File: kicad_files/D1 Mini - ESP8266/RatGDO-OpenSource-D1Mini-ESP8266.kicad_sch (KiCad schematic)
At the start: 7 parts, among them J1 Screw_Terminal_01x03, Q1 2N7002, Q2 AO3400A, U1 WeMos_D1_mini

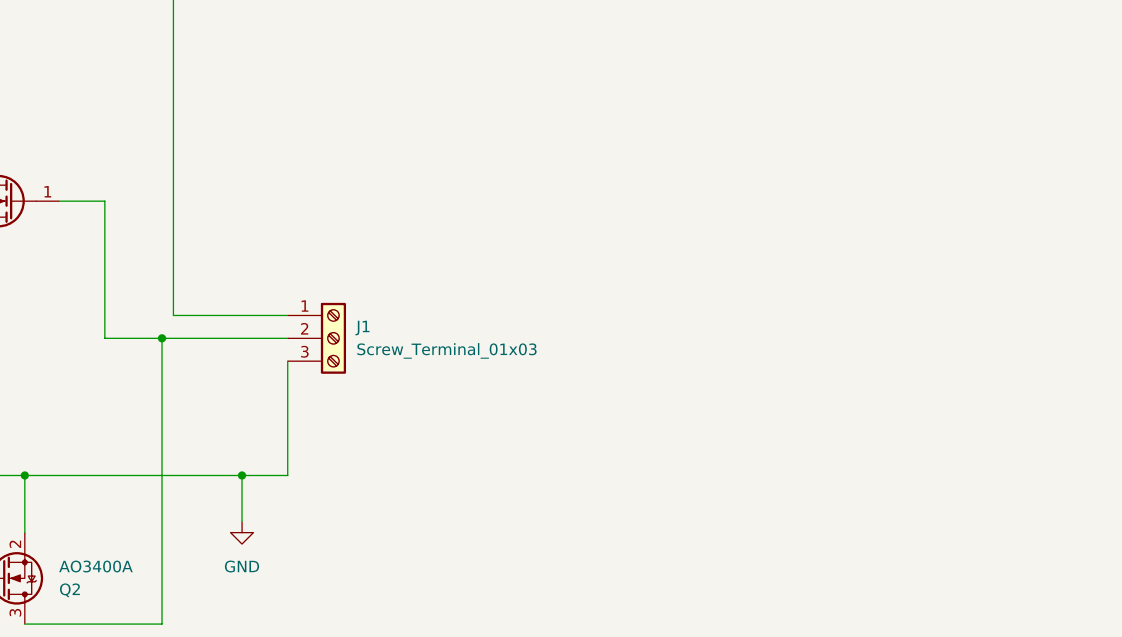
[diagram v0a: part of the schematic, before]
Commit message: Fixed Bad PCB Labeling
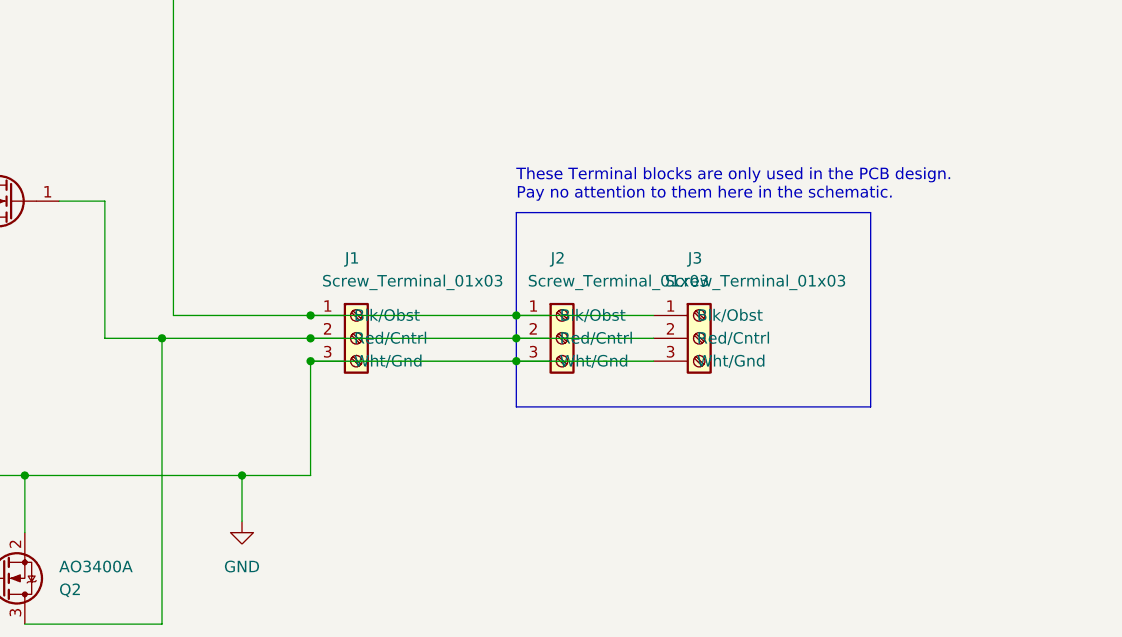
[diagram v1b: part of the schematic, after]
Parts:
- added J2: Screw_Terminal_01x03, Connector_Phoenix_MC:PhoenixContact_MCV_1,5_3-G-3.5_1x03_P3.50mm_Vertical, symbol Connector:Screw_Terminal_01x03
- added J3: Screw_Terminal_01x03, Connector_PinHeader_2.54mm:PinHeader_1x03_P2.54mm_Vertical, symbol Connector:Screw_Terminal_01x03
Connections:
- net GND: now also J2.3 (Wht/Gnd), J3.3 (Wht/Gnd)
- net at J1.1 (Blk/Obst), R1.1: now also J2.1 (Blk/Obst), J3.1 (Blk/Obst)
- net at J1.2 (Red/Cntrl), Q1.1 (G), Q2.3 (D): now also J2.2 (Red/Cntrl), J3.2 (Red/Cntrl)
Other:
- note added: "These Terminal blocks are only used in the PCB design. Pay no attention to them here in the schematic."
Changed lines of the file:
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@@
 (kicad_sch (version 20230121) (generator eeschema)
   (paper "A4")
+  (junction (at 160.02 87.63) (diameter 0) (color 0 0 0 0)
+  )
+  (junction (at 182.88 87.63) (diameter 0) (color 0 0 0 0)
+  )
   (junction (at 152.4 105.41) (diameter 0) (color 0 0 0 0)
   )
+  (junction (at 160.02 92.71) (diameter 0) (color 0 0 0 0)
+  )
   (junction (at 105.41 105.41) (diameter 0) (color 0 0 0 0)
   )
+  (junction (at 160.02 90.17) (diameter 0) (color 0 0 0 0)
+  )
   (junction (at 128.27 105.41) (diameter 0) (color 0 0 0 0)
   )
+  (junction (at 182.88 92.71) (diameter 0) (color 0 0 0 0)
+  )
+  (junction (at 182.88 90.17) (diameter 0) (color 0 0 0 0)
+  )
   (junction (at 105.41 69.85) (diameter 0) (color 0 0 0 0)
   )
@@
   (junction (at 105.41 116.84) (diameter 0) (color 0 0 0 0)
   )
+  (wire (pts (xy 182.88 87.63) (xy 198.12 87.63))
+    (stroke (width 0) (type default))
+  )
   (wire (pts (xy 128.27 121.92) (xy 143.51 121.92))
     (stroke (width 0) (type default))
@@
     (stroke (width 0) (type default))
   )
+  (polyline (pts (xy 182.88 76.2) (xy 222.25 76.2))
+    (stroke (width 0) (type default))
+  )
   (wire (pts (xy 143.51 90.17) (xy 137.16 90.17))
     (stroke (width 0) (type default))
@@
     (stroke (width 0) (type default))
   )
+  (wire (pts (xy 160.02 90.17) (xy 182.88 90.17))
+    (stroke (width 0) (type default))
+  )
   (wire (pts (xy 113.03 52.07) (xy 144.78 52.07))
     (stroke (width 0) (type default))
   )
+  (polyline (pts (xy 182.88 97.79) (xy 222.25 97.79))
+    (stroke (width 0) (type default))
+  )
   (wire (pts (xy 90.17 80.01) (xy 124.46 80.01))
     (stroke (width 0) (type default))
@@
     (stroke (width 0) (type default))
   )
+  (wire (pts (xy 160.02 87.63) (xy 182.88 87.63))
+    (stroke (width 0) (type default))
+  )
   (wire (pts (xy 105.41 52.07) (xy 95.25 52.07))
     (stroke (width 0) (type default))
@@
     (stroke (width 0) (type default))
   )
-  (wire (pts (xy 157.48 92.71) (xy 157.48 105.41))
+  (wire (pts (xy 160.02 92.71) (xy 160.02 105.41))
     (stroke (width 0) (type default))
   )
@@
     (stroke (width 0) (type default))
   )
+  (polyline (pts (xy 222.25 97.79) (xy 222.25 76.2))
+    (stroke (width 0) (type default))
+  )
   (wire (pts (xy 92.71 77.47) (xy 92.71 116.84))
     (stroke (width 0) (type default))
   )
+  (wire (pts (xy 160.02 92.71) (xy 182.88 92.71))
+    (stroke (width 0) (type default))
+  )
   (wire (pts (xy 152.4 105.41) (xy 152.4 110.49))
     (stroke (width 0) (type default))
@@
     (stroke (width 0) (type default))
   )
+  (wire (pts (xy 182.88 92.71) (xy 198.12 92.71))
+    (stroke (width 0) (type default))
+  )
   (wire (pts (xy 105.41 69.85) (xy 124.46 69.85))
     (stroke (width 0) (type default))
   )
+  (wire (pts (xy 182.88 90.17) (xy 198.12 90.17))
+    (stroke (width 0) (type default))
+  )
+  (polyline (pts (xy 182.88 76.2) (xy 182.88 97.79))
+    (stroke (width 0) (type default))
+  )
   (wire (pts (xy 82.55 57.15) (xy 82.55 64.77))
     (stroke (width 0) (type default))
@@
     (stroke (width 0) (type default))
   )
+  (wire (pts (xy 143.51 90.17) (xy 160.02 90.17))
+    (stroke (width 0) (type default))
+  )
   (wire (pts (xy 105.41 69.85) (xy 105.41 105.41))
     (stroke (width 0) (type default))
@@
     (stroke (width 0) (type default))
   )
-  (wire (pts (xy 144.78 87.63) (xy 157.48 87.63))
-    (stroke (width 0) (type default))
-  )
-  (wire (pts (xy 157.48 90.17) (xy 143.51 90.17))
+  (wire (pts (xy 144.78 87.63) (xy 160.02 87.63))
     (stroke (width 0) (type default))
   )
@@
     (stroke (width 0) (type default))
   )
-  (wire (pts (xy 157.48 105.41) (xy 152.4 105.41))
+  (wire (pts (xy 160.02 105.41) (xy 152.4 105.41))
     (stroke (width 0) (type default))
   )
   (wire (pts (xy 105.41 52.07) (xy 105.41 55.88))
     (stroke (width 0) (type default))
+  )
+  (text "These Terminal blocks are only used in the PCB design.\nPay no attention to them here in the schematic."
+    (at 182.88 74.93 0)
+    (effects (font (size 1.27 1.27)) (justify left bottom))
   )
   (symbol (lib_id "power:+5V") (at 77.47 57.15 0) (mirror x) (unit 1)
@@
     )
   )
-  (symbol (lib_id "Connector:Screw_Terminal_01x03") (at 162.56 90.17 0) (unit 1)
-    (in_bom yes) (on_board yes) (dnp no) (fields_autoplaced)
-    (property "Reference" "J1" (at 165.1 88.9 0)
-      (effects (font (size 1.27 1.27)) (justify left))
-    )
-    (property "Value" "Screw_Terminal_01x03" (at 165.1 91.44 0)
-      (effects (font (size 1.27 1.27)) (justify left))
-    )
-    (property "Footprint" "TerminalBlock_Phoenix:TerminalBlock_Phoenix_MKDS-1,5-3_1x03_P5.00mm_Horizontal" (at 162.56 90.17 0)
-      (effects (font (size 1.27 1.27)) hide)
-    )
-    (property "Datasheet" "~" (at 162.56 90.17 0)
+  (symbol (lib_id "Connector:Screw_Terminal_01x03") (at 165.1 90.17 0) (unit 1)
+    (in_bom yes) (on_board yes) (dnp no)
+    (property "Reference" "J1" (at 163.83 81.28 0)
+      (effects (font (size 1.27 1.27)) (justify left))
+    )
+    (property "Value" "Screw_Terminal_01x03" (at 161.29 83.82 0)
+      (effects (font (size 1.27 1.27)) (justify left))
+    )
+    (property "Footprint" "TerminalBlock_Phoenix:TerminalBlock_Phoenix_MKDS-1,5-3_1x03_P5.00mm_Horizontal" (at 165.1 90.17 0)
+      (effects (font (size 1.27 1.27)) hide)
+    )
+    (property "Datasheet" "~" (at 165.1 90.17 0)
       (effects (font (size 1.27 1.27)) hide)
     )
@@
         (path "/d526daf5-1a87-4c4a-b8db-6120ccadc008"
           (reference "J1") (unit 1)
+        )
+      )
+    )
+  )
+  (symbol (lib_id "Connector:Screw_Terminal_01x03") (at 203.2 90.17 0) (unit 1)
+    (in_bom yes) (on_board yes) (dnp no)
+    (property "Reference" "J3" (at 201.93 81.28 0)
+      (effects (font (size 1.27 1.27)) (justify left))
+    )
+    (property "Value" "Screw_Terminal_01x03" (at 199.39 83.82 0)
+      (effects (font (size 1.27 1.27)) (justify left))
+    )
+    (property "Footprint" "Connector_PinHeader_2.54mm:PinHeader_1x03_P2.54mm_Vertical" (at 203.2 90.17 0)
+      (effects (font (size 1.27 1.27)) hide)
+    )
+    (property "Datasheet" "~" (at 203.2 90.17 0)
+      (effects (font (size 1.27 1.27)) hide)
+    )
+    (pin "1")
+    (pin "2")
+    (pin "3")
+    (instances
+      (project "RatGDO-OpenSource-D1Mini-ESP8266"
+        (path "/d526daf5-1a87-4c4a-b8db-6120ccadc008"
+          (reference "J3") (unit 1)
         )
       )
@@
         )
       )
+    )
+  )
+  (symbol (lib_id "Connector:Screw_Terminal_01x03") (at 187.96 90.17 0) (unit 1)
+    (in_bom yes) (on_board yes) (dnp no)
+    (property "Reference" "J2" (at 186.69 81.28 0)
+      (effects (font (size 1.27 1.27)) (justify left))
+    )
+    (property "Value" "Screw_Terminal_01x03" (at 184.15 83.82 0)
+      (effects (font (size 1.27 1.27)) (justify left))
+    )
+    (property "Footprint" "Connector_Phoenix_MC:PhoenixContact_MCV_1,5_3-G-3.5_1x03_P3.50mm_Vertical" (at 187.96 90.17 0)
+      (effects (font (size 1.27 1.27)) hide)
+    )
+    (property "Datasheet" "~" (at 187.96 90.17 0)
+      (effects (font (size 1.27 1.27)) hide)
+    )
+    (pin "1")
+    (pin "2")
+    (pin "3")
+    (instances
+      (project "RatGDO-OpenSource-D1Mini-ESP8266"
+        (path "/d526daf5-1a87-4c4a-b8db-6120ccadc008"
+          (reference "J2") (unit 1)
+        )
+      )

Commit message: Change Pin Header to Pin Socket
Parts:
- J3: footprint Connector_PinHeader_2.54mm:PinHeader_1x03_P2.54mm_Vertical -> Connector_PinSocket_2.54mm:PinSocket_1x03_P2.54mm_Vertical
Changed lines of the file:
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@@
       (effects (font (size 1.27 1.27)) (justify left))
     )
-    (property "Footprint" "Connector_PinHeader_2.54mm:PinHeader_1x03_P2.54mm_Vertical" (at 203.2 90.17 0)
+    (property "Footprint" "Connector_PinSocket_2.54mm:PinSocket_1x03_P2.54mm_Vertical" (at 203.2 90.17 0)
       (effects (font (size 1.27 1.27)) hide)
     )

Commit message: Cleaning up Schematics and making PCB layout similar for D1 Boards
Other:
- moved on the sheet: Q1
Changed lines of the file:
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@@
   (junction (at 182.88 87.63) (diameter 0) (color 0 0 0 0)
   )
+  (junction (at 124.46 105.41) (diameter 0) (color 0 0 0 0)
+  )
   (junction (at 152.4 105.41) (diameter 0) (color 0 0 0 0)
   )
@@
   (junction (at 182.88 90.17) (diameter 0) (color 0 0 0 0)
   )
-  (junction (at 105.41 69.85) (diameter 0) (color 0 0 0 0)
-  )
   (junction (at 105.41 52.07) (diameter 0) (color 0 0 0 0)
   )
@@
     (stroke (width 0) (type default))
   )
+  (wire (pts (xy 124.46 105.41) (xy 128.27 105.41))
+    (stroke (width 0) (type default))
+  )
   (wire (pts (xy 128.27 121.92) (xy 143.51 121.92))
     (stroke (width 0) (type default))
   )
-  (wire (pts (xy 137.16 90.17) (xy 137.16 74.93))
-    (stroke (width 0) (type default))
-  )
-  (wire (pts (xy 132.08 74.93) (xy 137.16 74.93))
+  (wire (pts (xy 137.16 90.17) (xy 137.16 86.36))
+    (stroke (width 0) (type default))
+  )
+  (wire (pts (xy 132.08 86.36) (xy 137.16 86.36))
+    (stroke (width 0) (type default))
+  )
+  (wire (pts (xy 92.71 77.47) (xy 92.71 116.84))
     (stroke (width 0) (type default))
   )
@@
     (stroke (width 0) (type default))
   )
-  (wire (pts (xy 105.41 105.41) (xy 128.27 105.41))
+  (wire (pts (xy 105.41 105.41) (xy 124.46 105.41))
     (stroke (width 0) (type default))
   )
@@
     (stroke (width 0) (type default))
   )
+  (wire (pts (xy 144.78 52.07) (xy 144.78 87.63))
+    (stroke (width 0) (type default))
+  )
+  (wire (pts (xy 105.41 63.5) (xy 105.41 105.41))
+    (stroke (width 0) (type default))
+  )
+  (wire (pts (xy 160.02 87.63) (xy 182.88 87.63))
+    (stroke (width 0) (type default))
+  )
+  (wire (pts (xy 105.41 52.07) (xy 95.25 52.07))
+    (stroke (width 0) (type default))
+  )
+  (wire (pts (xy 152.4 105.41) (xy 128.27 105.41))
+    (stroke (width 0) (type default))
+  )
+  (wire (pts (xy 124.46 81.28) (xy 124.46 80.01))
+    (stroke (width 0) (type default))
+  )
+  (wire (pts (xy 160.02 92.71) (xy 160.02 105.41))
+    (stroke (width 0) (type default))
+  )
+  (wire (pts (xy 128.27 105.41) (xy 128.27 111.76))
+    (stroke (width 0) (type default))
+  )
+  (polyline (pts (xy 222.25 97.79) (xy 222.25 76.2))
+    (stroke (width 0) (type default))
+  )
+  (wire (pts (xy 160.02 92.71) (xy 182.88 92.71))
+    (stroke (width 0) (type default))
+  )
+  (wire (pts (xy 152.4 105.41) (xy 152.4 110.49))
+    (stroke (width 0) (type default))
+  )
+  (wire (pts (xy 92.71 116.84) (xy 105.41 116.84))
+    (stroke (width 0) (type default))
+  )
+  (wire (pts (xy 120.65 116.84) (xy 105.41 116.84))
+    (stroke (width 0) (type default))
+  )
+  (wire (pts (xy 77.47 57.15) (xy 77.47 64.77))
+    (stroke (width 0) (type default))
+  )
+  (wire (pts (xy 182.88 92.71) (xy 198.12 92.71))
+    (stroke (width 0) (type default))
+  )
+  (wire (pts (xy 182.88 90.17) (xy 198.12 90.17))
+    (stroke (width 0) (type default))
+  )
+  (polyline (pts (xy 182.88 76.2) (xy 182.88 97.79))
+    (stroke (width 0) (type default))
+  )
+  (wire (pts (xy 82.55 57.15) (xy 82.55 64.77))
+    (stroke (width 0) (type default))
+  )
+  (wire (pts (xy 105.41 116.84) (xy 105.41 113.03))
+    (stroke (width 0) (type default))
+  )
   (wire (pts (xy 90.17 80.01) (xy 124.46 80.01))
     (stroke (width 0) (type default))
   )
-  (wire (pts (xy 144.78 52.07) (xy 144.78 87.63))
-    (stroke (width 0) (type default))
-  )
-  (wire (pts (xy 105.41 63.5) (xy 105.41 69.85))
-    (stroke (width 0) (type default))
-  )
-  (wire (pts (xy 160.02 87.63) (xy 182.88 87.63))
-    (stroke (width 0) (type default))
-  )
-  (wire (pts (xy 105.41 52.07) (xy 95.25 52.07))
-    (stroke (width 0) (type default))
-  )
-  (wire (pts (xy 152.4 105.41) (xy 128.27 105.41))
-    (stroke (width 0) (type default))
-  )
-  (wire (pts (xy 160.02 92.71) (xy 160.02 105.41))
-    (stroke (width 0) (type default))
-  )
-  (wire (pts (xy 128.27 105.41) (xy 128.27 111.76))
-    (stroke (width 0) (type default))
-  )
-  (polyline (pts (xy 222.25 97.79) (xy 222.25 76.2))
-    (stroke (width 0) (type default))
-  )
-  (wire (pts (xy 92.71 77.47) (xy 92.71 116.84))
-    (stroke (width 0) (type default))
-  )
-  (wire (pts (xy 160.02 92.71) (xy 182.88 92.71))
-    (stroke (width 0) (type default))
-  )
-  (wire (pts (xy 152.4 105.41) (xy 152.4 110.49))
-    (stroke (width 0) (type default))
-  )
-  (wire (pts (xy 92.71 116.84) (xy 105.41 116.84))
+  (wire (pts (xy 143.51 90.17) (xy 160.02 90.17))
     (stroke (width 0) (type default))
   )
@@
     (stroke (width 0) (type default))
   )
-  (wire (pts (xy 120.65 116.84) (xy 105.41 116.84))
-    (stroke (width 0) (type default))
-  )
-  (wire (pts (xy 77.47 57.15) (xy 77.47 64.77))
-    (stroke (width 0) (type default))
-  )
-  (wire (pts (xy 182.88 92.71) (xy 198.12 92.71))
-    (stroke (width 0) (type default))
-  )
-  (wire (pts (xy 105.41 69.85) (xy 124.46 69.85))
-    (stroke (width 0) (type default))
-  )
-  (wire (pts (xy 182.88 90.17) (xy 198.12 90.17))
-    (stroke (width 0) (type default))
-  )
-  (polyline (pts (xy 182.88 76.2) (xy 182.88 97.79))
-    (stroke (width 0) (type default))
-  )
-  (wire (pts (xy 82.55 57.15) (xy 82.55 64.77))
-    (stroke (width 0) (type default))
-  )
-  (wire (pts (xy 105.41 116.84) (xy 105.41 113.03))
-    (stroke (width 0) (type default))
-  )
-  (wire (pts (xy 143.51 90.17) (xy 160.02 90.17))
-    (stroke (width 0) (type default))
-  )
-  (wire (pts (xy 105.41 69.85) (xy 105.41 105.41))
-    (stroke (width 0) (type default))
-  )
   (wire (pts (xy 80.01 105.41) (xy 105.41 105.41))
     (stroke (width 0) (type default))
@@
   )
   (wire (pts (xy 160.02 105.41) (xy 152.4 105.41))
+    (stroke (width 0) (type default))
+  )
+  (wire (pts (xy 124.46 91.44) (xy 124.46 105.41))
     (stroke (width 0) (type default))
   )
@@
     )
   )
-  (symbol (lib_id "Transistor_FET:2N7002") (at 127 74.93 180) (unit 1)
-    (in_bom yes) (on_board yes) (dnp no)
-    (property "Reference" "Q1" (at 120.65 76.2 0)
-      (effects (font (size 1.27 1.27)) (justify left))
-    )
-    (property "Value" "2N7002" (at 120.65 73.66 0)
-      (effects (font (size 1.27 1.27)) (justify left))
-    )
-    (property "Footprint" "Package_TO_SOT_SMD:SOT-23" (at 121.92 73.025 0)
+  (symbol (lib_id "Transistor_FET:2N7002") (at 127 86.36 0) (mirror y) (unit 1)
+    (in_bom yes) (on_board yes) (dnp no)
+    (property "Reference" "Q1" (at 120.65 85.09 0)
+      (effects (font (size 1.27 1.27)) (justify left))
+    )
+    (property "Value" "2N7002" (at 120.65 87.63 0)
+      (effects (font (size 1.27 1.27)) (justify left))
+    )
+    (property "Footprint" "Package_TO_SOT_SMD:SOT-23" (at 121.92 88.265 0)
       (effects (font (size 1.27 1.27) italic) (justify left) hide)
     )
-    (property "Datasheet" "https://www.onsemi.com/pub/Collateral/NDS7002A-D.PDF" (at 127 74.93 0)
+    (property "Datasheet" "https://www.onsemi.com/pub/Collateral/NDS7002A-D.PDF" (at 127 86.36 0)
       (effects (font (size 1.27 1.27)) (justify left) hide)
     )

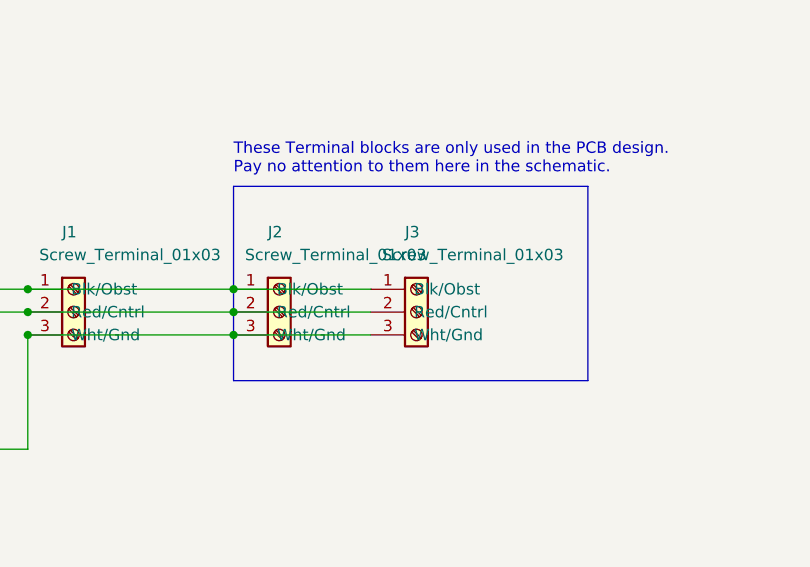
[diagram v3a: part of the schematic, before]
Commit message: Added Bare ESP8266 kicad files.
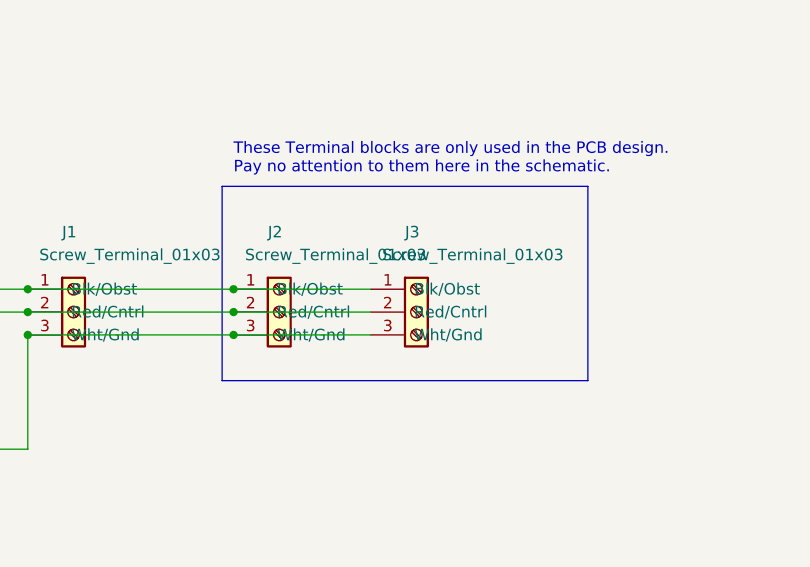
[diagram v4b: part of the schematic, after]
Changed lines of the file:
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@@
     (stroke (width 0) (type default))
   )
-  (polyline (pts (xy 182.88 76.2) (xy 222.25 76.2))
+  (polyline (pts (xy 181.61 76.2) (xy 222.25 76.2))
     (stroke (width 0) (type default))
   )
@@
     (stroke (width 0) (type default))
   )
-  (polyline (pts (xy 182.88 97.79) (xy 222.25 97.79))
+  (polyline (pts (xy 181.61 97.79) (xy 222.25 97.79))
     (stroke (width 0) (type default))
   )
@@
     (stroke (width 0) (type default))
   )
-  (polyline (pts (xy 182.88 76.2) (xy 182.88 97.79))
+  (polyline (pts (xy 181.61 76.2) (xy 181.61 97.79))
     (stroke (width 0) (type default))
   )
